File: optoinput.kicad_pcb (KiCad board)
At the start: 2 copper layers, 76.2 x 50.8 mm, 32 parts, among them P1 CONN_01X08, P2 CONN_01X08, P3 CONN_01X03, P6 CONN_01X02, U1 4N25, U2 4N25, U3 4N25, U4 4N25, U5 4N25, U6 4N25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

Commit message: single layer mod
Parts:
- REF** (x4): value SolderWirePad_single_2mmDrill -> 2mm
- moved REF** 3.74 mm to (102.2, 48.6)
- moved REF** 3.68 mm to (36.8, 48.6)
- moved R13 2.65 mm to (86.4, 91.3), turned to 270 degrees
- moved R14 2.65 mm to (73.0, 91.3), turned to 270 degrees
- moved R15 2.65 mm to (59.7, 91.3), turned to 270 degrees
- moved R16 2.65 mm to (46.4, 91.3), turned to 270 degrees
- moved R6 2.54 mm to (64.8, 56.5), turned to 90 degrees
- moved R8 2.54 mm to (91.4, 56.5), turned to 90 degrees
- moved R5 2.54 mm to (51.4, 56.5), turned to 90 degrees
- moved R7 2.54 mm to (78.1, 56.5), turned to 90 degrees
- moved REF** 1.65 mm to (102.2, 98.9)
- moved REF** 1.65 mm to (36.8, 99.1)
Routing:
- net /Y5: track 32.1 -> 23.5 mm
- net /Y6: track 43.6 -> 35.4 mm
- net /Y8: track 67.7 -> 60.4 mm
- net /Y7: track 55.6 -> 48.8 mm
- net /Y4: track 29.2 -> 36.0 mm
- net /Y1: track 66.5 -> 72.1 mm
- net /Y2: track 55.1 -> 59.9 mm
- net /Y3: track 44.2 -> 48.3 mm
- net VCC: track 202.8 -> 205.6 mm
- removed copper zone on B.Cu, net GND
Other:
- board size 76.2 x 50.8 mm -> 75.4 x 58.8 mm

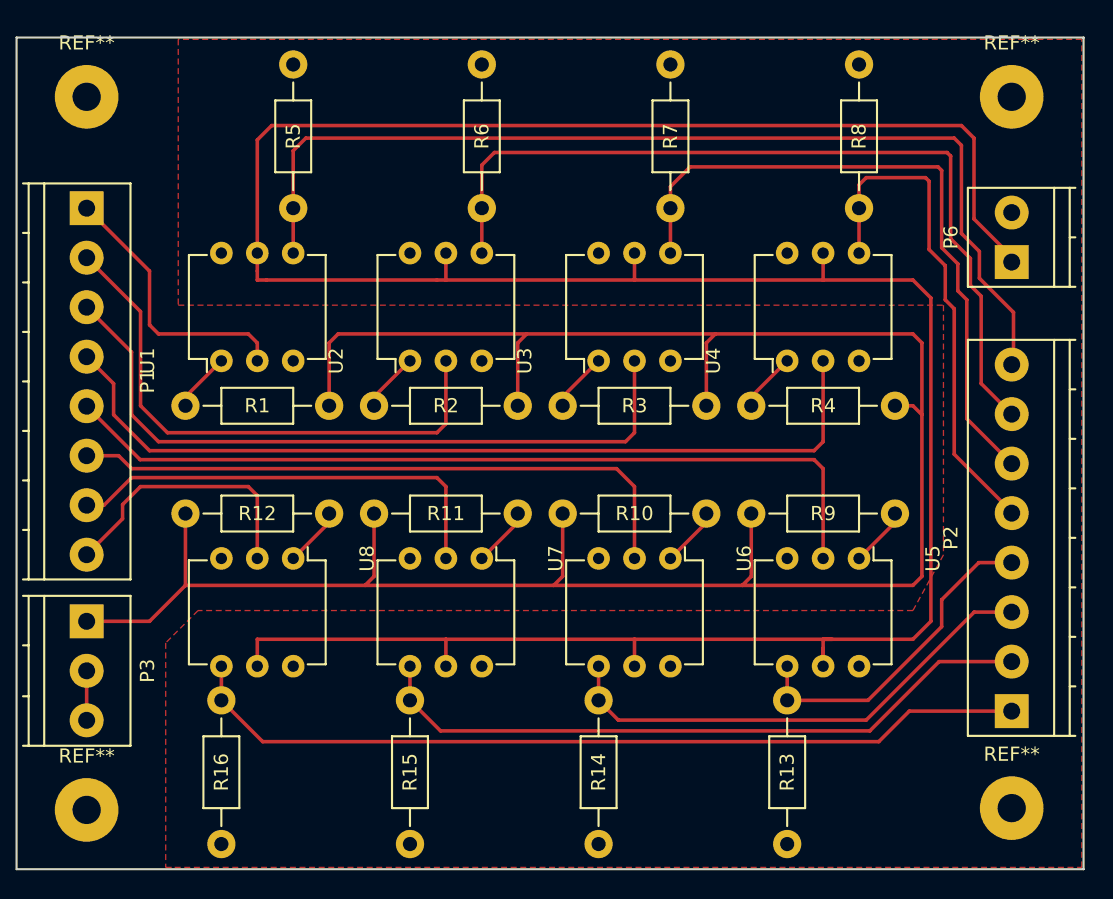
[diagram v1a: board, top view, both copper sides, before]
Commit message: moved tracks/zones to back layer
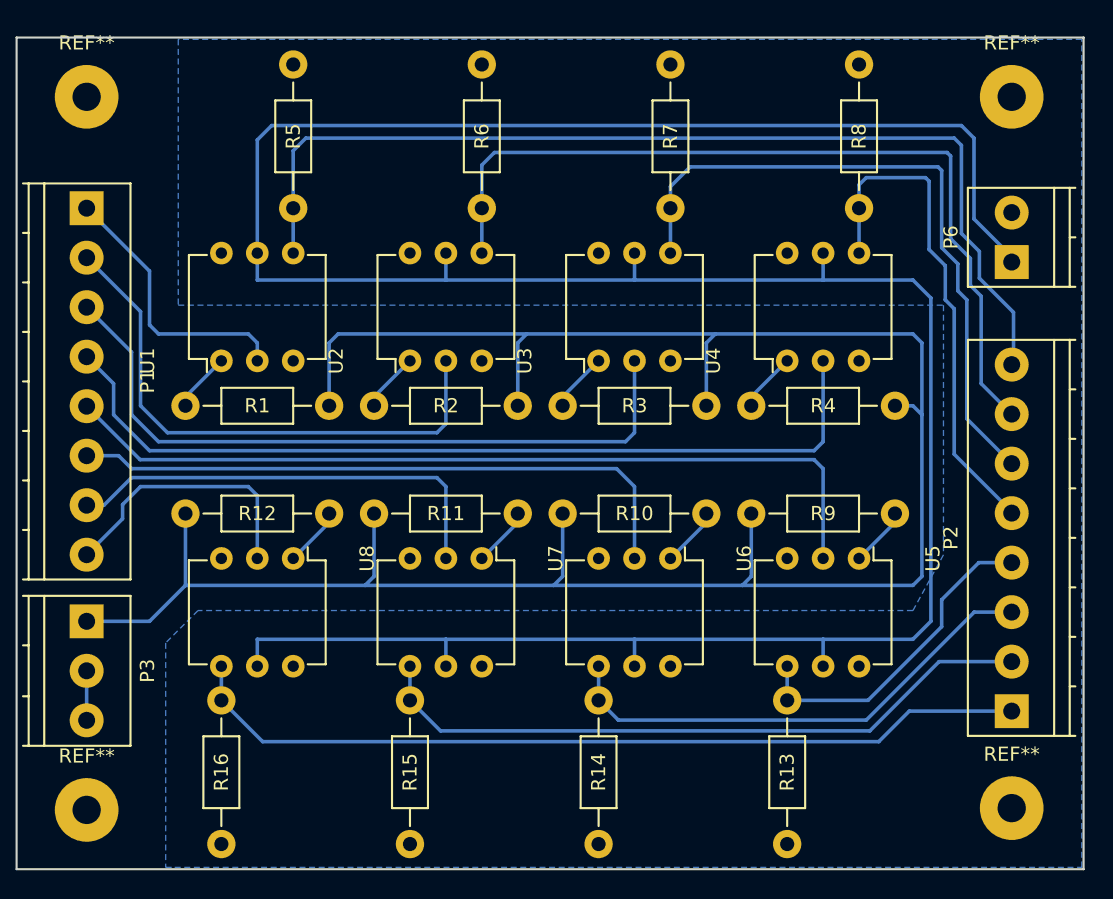
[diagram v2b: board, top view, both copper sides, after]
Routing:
- net VCC: track 205.6 -> 203.7 mm
- added copper zone on B.Cu, net GND
- removed copper zone on F.Cu, net GND

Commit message: removed fill zone, changed plot to PDF(mirrored), more separation between +12 and +5 zones
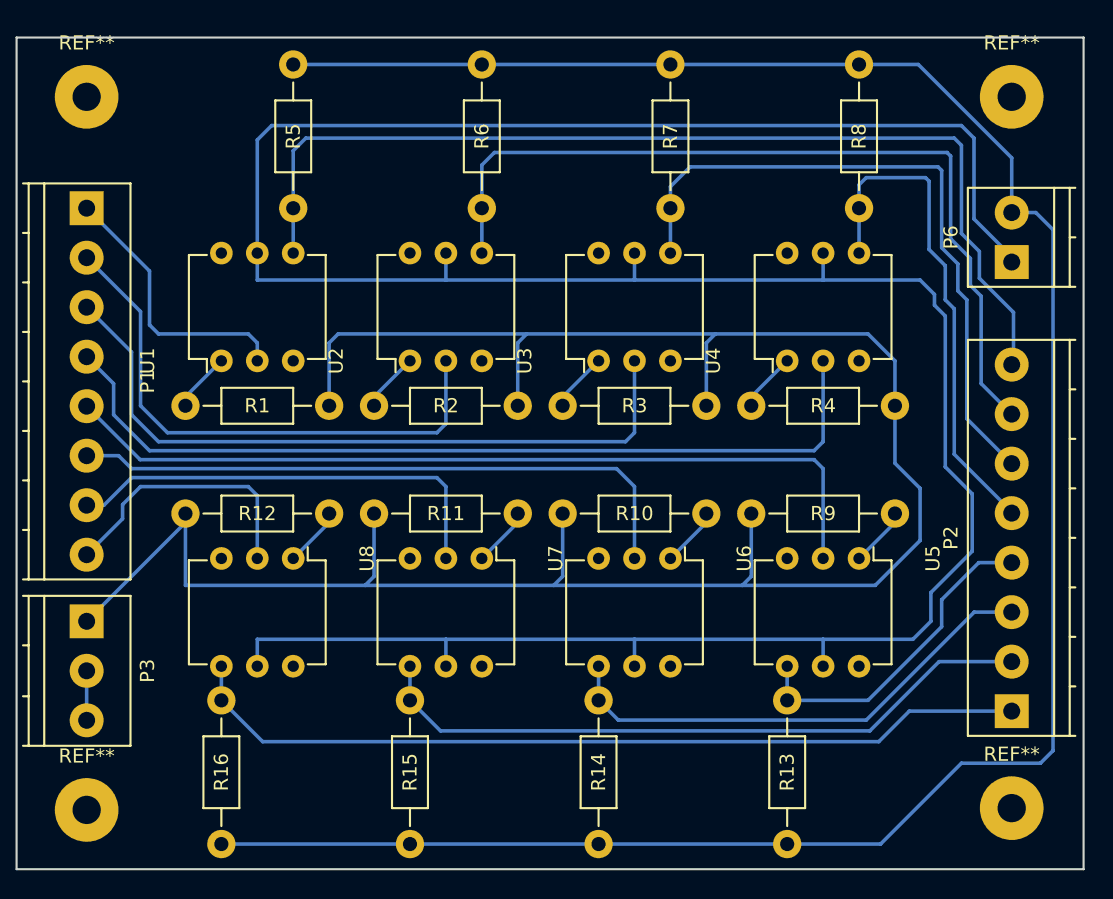
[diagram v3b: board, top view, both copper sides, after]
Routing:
- net GND: track 0.00 -> 159.2 mm
- net +12V: track 157.7 -> 154.5 mm
- net VCC: track 203.7 -> 206.5 mm
- removed copper zone on B.Cu, net GND
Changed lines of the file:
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@@
     (thickness 1.6)
     (drawings 4)
-    (tracks 190)
+    (tracks 212)
     (zones 0)
     (modules 32)
@@
     (visible_elements FFFFFF7F)
     (pcbplotparams
-      (layerselection 0x01030_80000001)
+      (layerselection 0x00000_80000000)
       (usegerberextensions false)
-      (excludeedgelayer true)
+      (excludeedgelayer false)
       (linewidth 0.100000)
       (plotframeref false)
@@
       (padsonsilk false)
       (subtractmaskfromsilk false)
-      (outputformat 1)
-      (mirror false)
-      (drillshape 0)
+      (outputformat 4)
+      (mirror true)
+      (drillshape 2)
       (scaleselection 1)
       (outputdirectory plot/))
@@
   (segment (start 94.996 92.075) (end 92.837 94.234) (width 0.254) (layer B.Cu) (net 16))
   (segment (start 46.355 88.9) (end 46.355 91.313) (width 0.254) (layer B.Cu) (net 16) (status 30))
+  (segment (start 93.98 70.485) (end 93.98 74.549) (width 0.254) (layer B.Cu) (net 17) (status 10))
+  (segment (start 92.583 83.185) (end 83.185 83.185) (width 0.254) (layer B.Cu) (net 17))
+  (segment (start 95.758 80.01) (end 92.583 83.185) (width 0.254) (layer B.Cu) (net 17))
+  (segment (start 95.758 76.327) (end 95.758 80.01) (width 0.254) (layer B.Cu) (net 17))
+  (segment (start 93.98 74.549) (end 95.758 76.327) (width 0.254) (layer B.Cu) (net 17))
+  (segment (start 93.98 70.485) (end 93.98 67.31) (width 0.254) (layer B.Cu) (net 17) (status 10))
+  (segment (start 92.075 65.405) (end 81.28 65.405) (width 0.254) (layer B.Cu) (net 17))
+  (segment (start 93.98 67.31) (end 92.075 65.405) (width 0.254) (layer B.Cu) (net 17))
+  (segment (start 43.815 78.105) (end 43.815 78.74) (width 0.254) (layer B.Cu) (net 17) (status 30))
+  (segment (start 43.815 78.74) (end 36.83 85.725) (width 0.254) (layer B.Cu) (net 17) (status 30))
   (segment (start 67.945 65.405) (end 54.61 65.405) (width 0.254) (layer B.Cu) (net 17))
   (segment (start 53.975 66.04) (end 53.975 70.485) (width 0.254) (layer B.Cu) (net 17) (status 20))
   (segment (start 54.61 65.405) (end 53.975 66.04) (width 0.254) (layer B.Cu) (net 17))
   (segment (start 67.31 66.04) (end 67.31 70.485) (width 0.254) (layer B.Cu) (net 17) (status 20))
-  (segment (start 83.185 83.185) (end 95.25 83.185) (width 0.254) (layer B.Cu) (net 17))
-  (segment (start 95.25 70.485) (end 93.98 70.485) (width 0.254) (layer B.Cu) (net 17) (status 20))
-  (segment (start 95.885 71.12) (end 95.25 70.485) (width 0.254) (layer B.Cu) (net 17))
-  (segment (start 95.885 82.55) (end 95.885 71.12) (width 0.254) (layer B.Cu) (net 17))
-  (segment (start 95.25 83.185) (end 95.885 82.55) (width 0.254) (layer B.Cu) (net 17))
   (segment (start 69.85 83.185) (end 83.185 83.185) (width 0.254) (layer B.Cu) (net 17))
   (segment (start 83.82 82.55) (end 83.82 78.105) (width 0.254) (layer B.Cu) (net 17) (status 20))
@@
   (segment (start 57.15 82.55) (end 57.15 78.105) (width 0.254) (layer B.Cu) (net 17) (status 20))
   (segment (start 56.515 83.185) (end 57.15 82.55) (width 0.254) (layer B.Cu) (net 17))
-  (segment (start 36.83 85.725) (end 41.275 85.725) (width 0.254) (layer B.Cu) (net 17) (status 10))
   (segment (start 43.815 83.185) (end 43.815 78.105) (width 0.254) (layer B.Cu) (net 17) (status 20))
-  (segment (start 41.275 85.725) (end 43.815 83.185) (width 0.254) (layer B.Cu) (net 17))
   (segment (start 81.28 65.405) (end 67.945 65.405) (width 0.254) (layer B.Cu) (net 17))
   (segment (start 67.945 65.405) (end 67.31 66.04) (width 0.254) (layer B.Cu) (net 17))
-  (segment (start 95.885 71.12) (end 95.885 66.04) (width 0.254) (layer B.Cu) (net 17))
   (segment (start 80.645 66.04) (end 80.645 70.485) (width 0.254) (layer B.Cu) (net 17) (status 20))
   (segment (start 81.28 65.405) (end 80.645 66.04) (width 0.254) (layer B.Cu) (net 17))
-  (segment (start 95.25 65.405) (end 81.28 65.405) (width 0.254) (layer B.Cu) (net 17))
-  (segment (start 95.885 66.04) (end 95.25 65.405) (width 0.254) (layer B.Cu) (net 17))
+  (segment (start 88.9 61.595) (end 95.758 61.595) (width 0.254) (layer B.Cu) (net 18))
+  (segment (start 95.25 86.995) (end 88.9 86.995) (width 0.254) (layer B.Cu) (net 18))
+  (segment (start 96.52 85.725) (end 95.25 86.995) (width 0.254) (layer B.Cu) (net 18))
+  (segment (start 96.52 83.693) (end 96.52 85.725) (width 0.254) (layer B.Cu) (net 18))
+  (segment (start 99.441 80.772) (end 96.52 83.693) (width 0.254) (layer B.Cu) (net 18))
+  (segment (start 99.441 76.708) (end 99.441 80.772) (width 0.254) (layer B.Cu) (net 18))
+  (segment (start 97.536 74.803) (end 99.441 76.708) (width 0.254) (layer B.Cu) (net 18))
+  (segment (start 97.536 64.135) (end 97.536 74.803) (width 0.254) (layer B.Cu) (net 18))
+  (segment (start 96.774 63.373) (end 97.536 64.135) (width 0.254) (layer B.Cu) (net 18))
+  (segment (start 96.774 62.611) (end 96.774 63.373) (width 0.254) (layer B.Cu) (net 18))
+  (segment (start 95.758 61.595) (end 96.774 62.611) (width 0.254) (layer B.Cu) (net 18))
   (segment (start 102.235 60.325) (end 102.235 59.944) (width 0.254) (layer B.Cu) (net 18) (status 30))
   (segment (start 102.235 59.944) (end 99.568 57.277) (width 0.254) (layer B.Cu) (net 18) (status 10))
@@
   (segment (start 48.895 51.689) (end 48.895 59.69) (width 0.254) (layer B.Cu) (net 18) (status 20))
   (segment (start 48.895 59.69) (end 48.895 61.595) (width 0.254) (layer B.Cu) (net 18) (status 10))
-  (segment (start 95.25 86.995) (end 88.9 86.995) (width 0.254) (layer B.Cu) (net 18))
   (segment (start 88.9 88.9) (end 88.9 86.995) (width 0.254) (layer B.Cu) (net 18) (status 10))
   (segment (start 75.565 86.995) (end 88.9 86.995) (width 0.254) (layer B.Cu) (net 18))
@@
   (segment (start 62.23 86.995) (end 62.23 88.9) (width 0.254) (layer B.Cu) (net 18) (status 20))
   (segment (start 48.895 86.995) (end 62.23 86.995) (width 0.254) (layer B.Cu) (net 18))
-  (segment (start 95.25 61.595) (end 88.9 61.595) (width 0.254) (layer B.Cu) (net 18))
-  (segment (start 95.25 86.995) (end 96.52 85.725) (width 0.254) (layer B.Cu) (net 18))
-  (segment (start 96.52 85.725) (end 96.52 62.865) (width 0.254) (layer B.Cu) (net 18))
-  (segment (start 96.52 62.865) (end 95.25 61.595) (width 0.254) (layer B.Cu) (net 18))
   (segment (start 75.565 61.595) (end 88.9 61.595) (width 0.254) (layer B.Cu) (net 18))
   (segment (start 88.9 61.595) (end 88.9 59.69) (width 0.254) (layer B.Cu) (net 18) (status 20))
@@
   (segment (start 62.23 61.595) (end 62.23 59.69) (width 0.254) (layer B.Cu) (net 18) (status 20))
   (segment (start 48.895 61.595) (end 62.23 61.595) (width 0.254) (layer B.Cu) (net 18))
+  (segment (start 73.025 101.473) (end 86.36 101.473) (width 0.254) (layer B.Cu) (net 19))
+  (segment (start 86.36 101.473) (end 92.964 101.473) (width 0.254) (layer B.Cu) (net 19))
+  (segment (start 103.942 56.825) (end 102.235 56.825) (width 0.254) (layer B.Cu) (net 19) (status 20))
+  (segment (start 105.156 58.039) (end 103.942 56.825) (width 0.254) (layer B.Cu) (net 19))
+  (segment (start 105.156 94.869) (end 105.156 58.039) (width 0.254) (layer B.Cu) (net 19))
+  (segment (start 104.267 95.758) (end 105.156 94.869) (width 0.254) (layer B.Cu) (net 19))
+  (segment (start 98.679 95.758) (end 104.267 95.758) (width 0.254) (layer B.Cu) (net 19))
+  (segment (start 92.964 101.473) (end 98.679 95.758) (width 0.254) (layer B.Cu) (net 19) (status 10))
+  (segment (start 78.105 46.355) (end 91.44 46.355) (width 0.254) (layer B.Cu) (net 19) (status 30))
+  (segment (start 102.235 56.825) (end 102.235 52.959) (width 0.254) (layer B.Cu) (net 19) (status 10))
+  (segment (start 102.235 52.959) (end 95.631 46.355) (width 0.254) (layer B.Cu) (net 19))
+  (segment (start 95.631 46.355) (end 91.44 46.355) (width 0.254) (layer B.Cu) (net 19) (status 20))
+  (segment (start 78.105 46.355) (end 64.77 46.355) (width 0.254) (layer B.Cu) (net 19) (status 30))
+  (segment (start 64.77 46.355) (end 51.435 46.355) (width 0.254) (layer B.Cu) (net 19) (status 30))
+  (segment (start 46.355 101.473) (end 59.69 101.473) (width 0.254) (layer B.Cu) (net 19) (status 30))
+  (segment (start 59.69 101.473) (end 73.025 101.473) (width 0.254) (layer B.Cu) (net 19) (status 30))
   (segment (start 43.815 70.485) (end 43.815 69.85) (width 0.254) (layer B.Cu) (net 20) (status 30))
   (segment (start 43.815 69.85) (end 46.355 67.31) (width 0.254) (layer B.Cu) (net 20) (status 30))
@@
   (segment (start 53.975 78.74) (end 51.435 81.28) (width 0.254) (layer B.Cu) (net 27) (status 30))
   (segment (start 36.83 89.225) (end 36.83 92.725) (width 0.254) (layer B.Cu) (net 28) (status 30))
-  (zone (net 19) (net_name GND) (layer B.Cu) (hatch edge 0.508)
-    (connect_pads (clearance 0.508))
-    (min_thickness 0.254)
-    (fill yes (arc_segments 16) (thermal_gap 0.508) (thermal_bridge_width 0.508))
-    (polygon
-      (pts
-        (xy 43.053 103.124) (xy 107.188 103.124) (xy 107.188 44.577) (xy 43.307 44.577) (xy 43.307 63.373)
-        (xy 97.409 63.373) (xy 97.409 81.026) (xy 95.25 84.963) (xy 44.704 84.963) (xy 42.418 87.249)
-        (xy 42.418 103.124) (xy 43.053 103.124)
-      )
-    )
-  )
 )

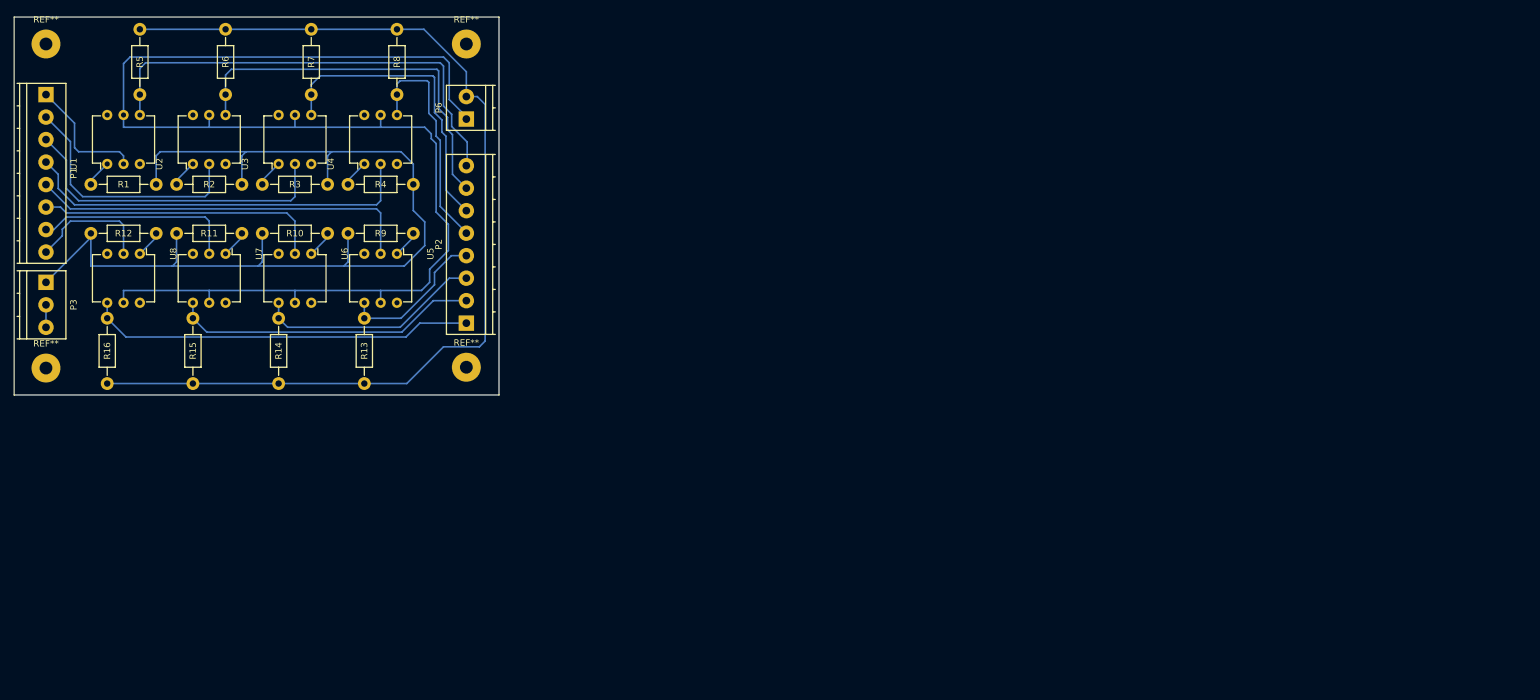
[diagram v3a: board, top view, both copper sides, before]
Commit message: changed to PS plot, clean up tracks
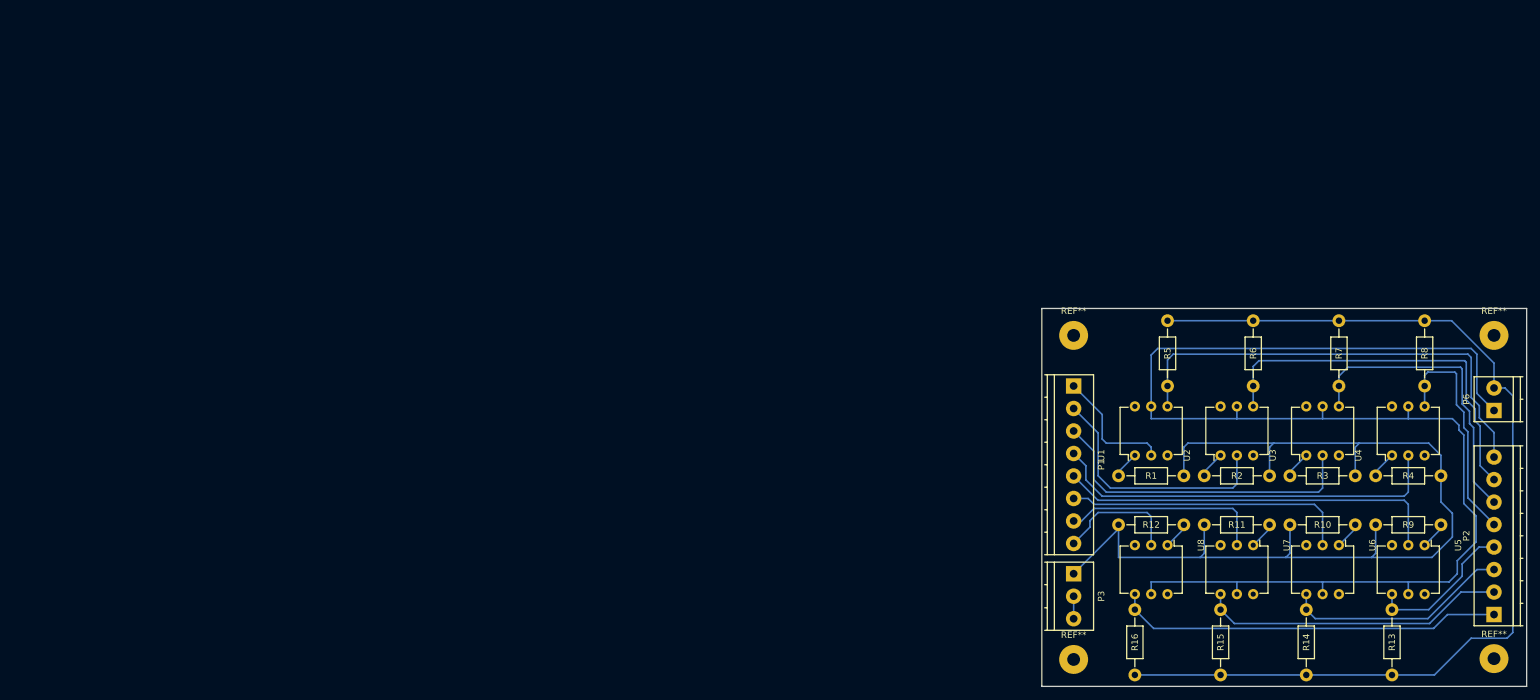
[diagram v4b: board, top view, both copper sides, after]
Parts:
- moved P1 166.2 mm to (196.7, 101.9)
- moved P3 166.2 mm to (196.7, 131.1)
- moved R3 166.2 mm to (240.5, 115.8)
- moved R6 166.2 mm to (224.7, 101.9)
- moved REF** 166.2 mm to (196.7, 94.0)
- moved REF** 166.2 mm to (196.7, 144.4)
- moved U7 166.2 mm to (224.7, 126.6)
- moved R1 166.2 mm to (213.9, 115.8)
- moved R11 166.2 mm to (217.0, 123.4)
- moved R12 166.2 mm to (203.7, 123.4)
- moved R14 166.2 mm to (232.9, 136.7)
- moved R15 166.2 mm to (219.6, 136.7)
- moved R16 166.2 mm to (206.2, 136.7)
- moved R2 166.2 mm to (227.2, 115.8)
- moved R5 166.2 mm to (211.3, 101.9)
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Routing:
- net /Y3: track 48.3 -> 47.3 mm
- net /Y7: track 48.8 -> 47.9 mm
- net /X3: track 51.3 -> 50.6 mm
